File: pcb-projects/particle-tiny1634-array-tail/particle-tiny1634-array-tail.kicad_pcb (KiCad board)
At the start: 2 copper layers, 71.2 x 8.1 mm, 4 parts, among them P1 CONN_02X03, P2 CONN_02X03, P3 CONN_02X03, P4 CONN_02X03

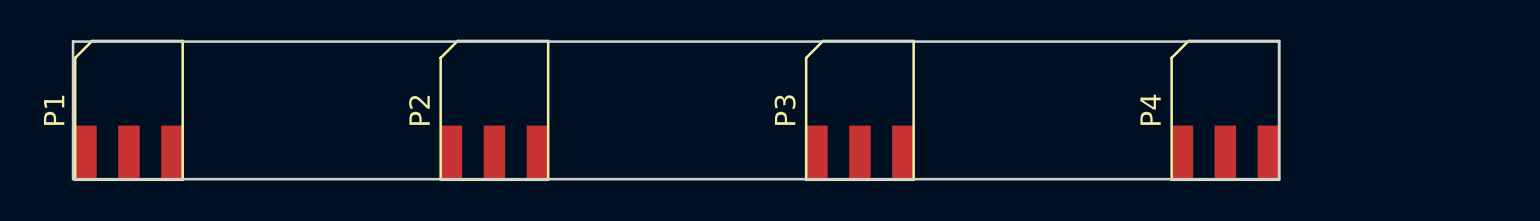
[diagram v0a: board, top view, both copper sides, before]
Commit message: minor edge cut alignment, added particle array
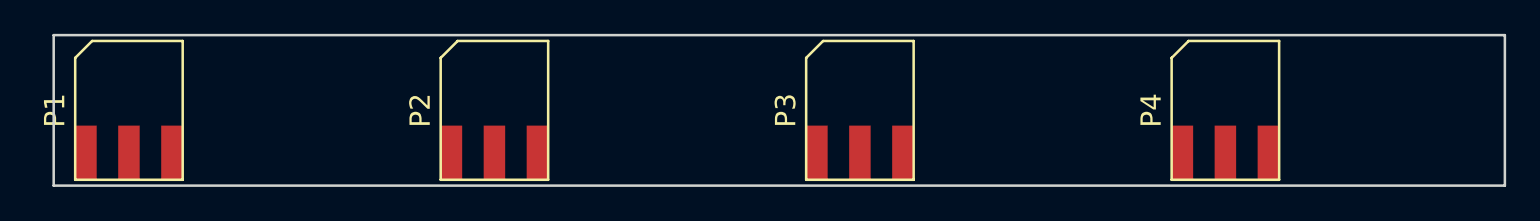
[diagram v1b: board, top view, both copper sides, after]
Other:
- board size 71.2 x 8.1 mm -> 85.7 x 8.9 mm
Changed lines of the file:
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@@
     (links 0)
     (no_connects 0)
-    (area 126.924999 98.476999 199.211001 107.263001)
+    (area 109.779999 97.079999 195.655001 106.120001)
     (thickness 1.6)
     (drawings 4)
@@
       (effects (font (size 1.2 1.2) (thickness 0.15)))
     )
-    (fp_text value CONN_02X03 (at 0 6.096) (layer F.Fab)
+    (fp_text value CONN_02X03 (at 0 -0.635) (layer F.Fab)
       (effects (font (size 1.2 1.2) (thickness 0.15)))
     )
@@
       (effects (font (size 1.2 1.2) (thickness 0.15)))
     )
-    (fp_text value CONN_02X03 (at 0 6.096) (layer F.Fab)
+    (fp_text value CONN_02X03 (at 0 -0.635) (layer F.Fab)
       (effects (font (size 1.2 1.2) (thickness 0.15)))
     )
@@
       (effects (font (size 1.2 1.2) (thickness 0.15)))
     )
-    (fp_text value CONN_02X03 (at 0 6.096) (layer F.Fab)
+    (fp_text value CONN_02X03 (at 0 -0.635) (layer F.Fab)
       (effects (font (size 1.2 1.2) (thickness 0.15)))
     )
@@
       (effects (font (size 1.2 1.2) (thickness 0.15)))
     )
-    (fp_text value CONN_02X03 (at 0 6.096) (layer F.Fab)
+    (fp_text value CONN_02X03 (at 0 -0.635) (layer F.Fab)
       (effects (font (size 1.2 1.2) (thickness 0.15)))
     )
@@
     )
   )
-  (gr_line (start 182.245 105.664) (end 110.998 105.664) (layer Edge.Cuts) (width 0.15))
-  (gr_line (start 182.245 97.536) (end 182.245 105.664) (layer Edge.Cuts) (width 0.15))
-  (gr_line (start 110.998 97.536) (end 182.245 97.536) (layer Edge.Cuts) (width 0.15))
-  (gr_line (start 110.998 105.664) (end 110.998 97.536) (layer Edge.Cuts) (width 0.15))
+  (gr_line (start 195.58 97.155) (end 195.58 106.045) (layer Edge.Cuts) (width 0.15))
+  (gr_line (start 109.855 97.155) (end 109.855 106.045) (layer Edge.Cuts) (width 0.15))
+  (gr_line (start 195.58 106.045) (end 109.855 106.045) (layer Edge.Cuts) (width 0.15))
+  (gr_line (start 109.855 97.155) (end 195.58 97.155) (layer Edge.Cuts) (width 0.15))
 )
